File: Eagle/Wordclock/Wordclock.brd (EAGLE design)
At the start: 130 x 130 mm, 266 parts, among them IC1 MEGA8-P, Q3 SUP75N06-08

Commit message: layout der leds
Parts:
- added PAD3, PAD4: (no value), wirepad:2,54/1,1
- R1, R2: device rcl:M0805 -> rcl:R1206
- moved Q2 39.5 mm to (-2.74, 69.5), turned to 90 degrees
- moved SV1 34.0 mm to (7.23, 109.6), turned to 90 degrees
- moved R_LED4 20.4 mm to (33.0, 123.9)
- moved R1 18.6 mm to (50.3, 122.0)
- moved R2 17.8 mm to (43.0, 121.5), turned to 0 degrees
- moved Q1 11.6 mm to (52.3, 116.6)
- moved S+1 8.66 mm to (40.5, 120.2), turned to 0 degrees
- turned IC1 to 90 degrees
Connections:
- net GND: now also PAD4.1
- net VDD: now also PAD3.1
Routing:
- net SCL: track 0.00 -> 39.6 mm
- net SDA: track 0.00 -> 38.0 mm
- net SCHALTER1: track 38.5 -> 2.70 mm
- net +5V: track 244.0 -> 278.0 mm
- net GND: track 1683.2 -> 1654.1 mm
- net N$117: track 0.00 -> 21.7 mm
- net LEDMIN1: track 118.1 -> 136.0 mm
- net N$127: track 109.7 -> 124.8 mm
- net MATRIXIN: track 0.00 -> 14.3 mm
- net INTA: track 0.00 -> 13.6 mm
- net LEDALARM: track 46.6 -> 39.7 mm
- net LEDMIN4: track 0.00 -> 5.52 mm
- net N$20: track 11.0 -> 5.65 mm
- net INTB: track 0.00 -> 2.75 mm
- net N$21: track 16.4 -> 14.6 mm

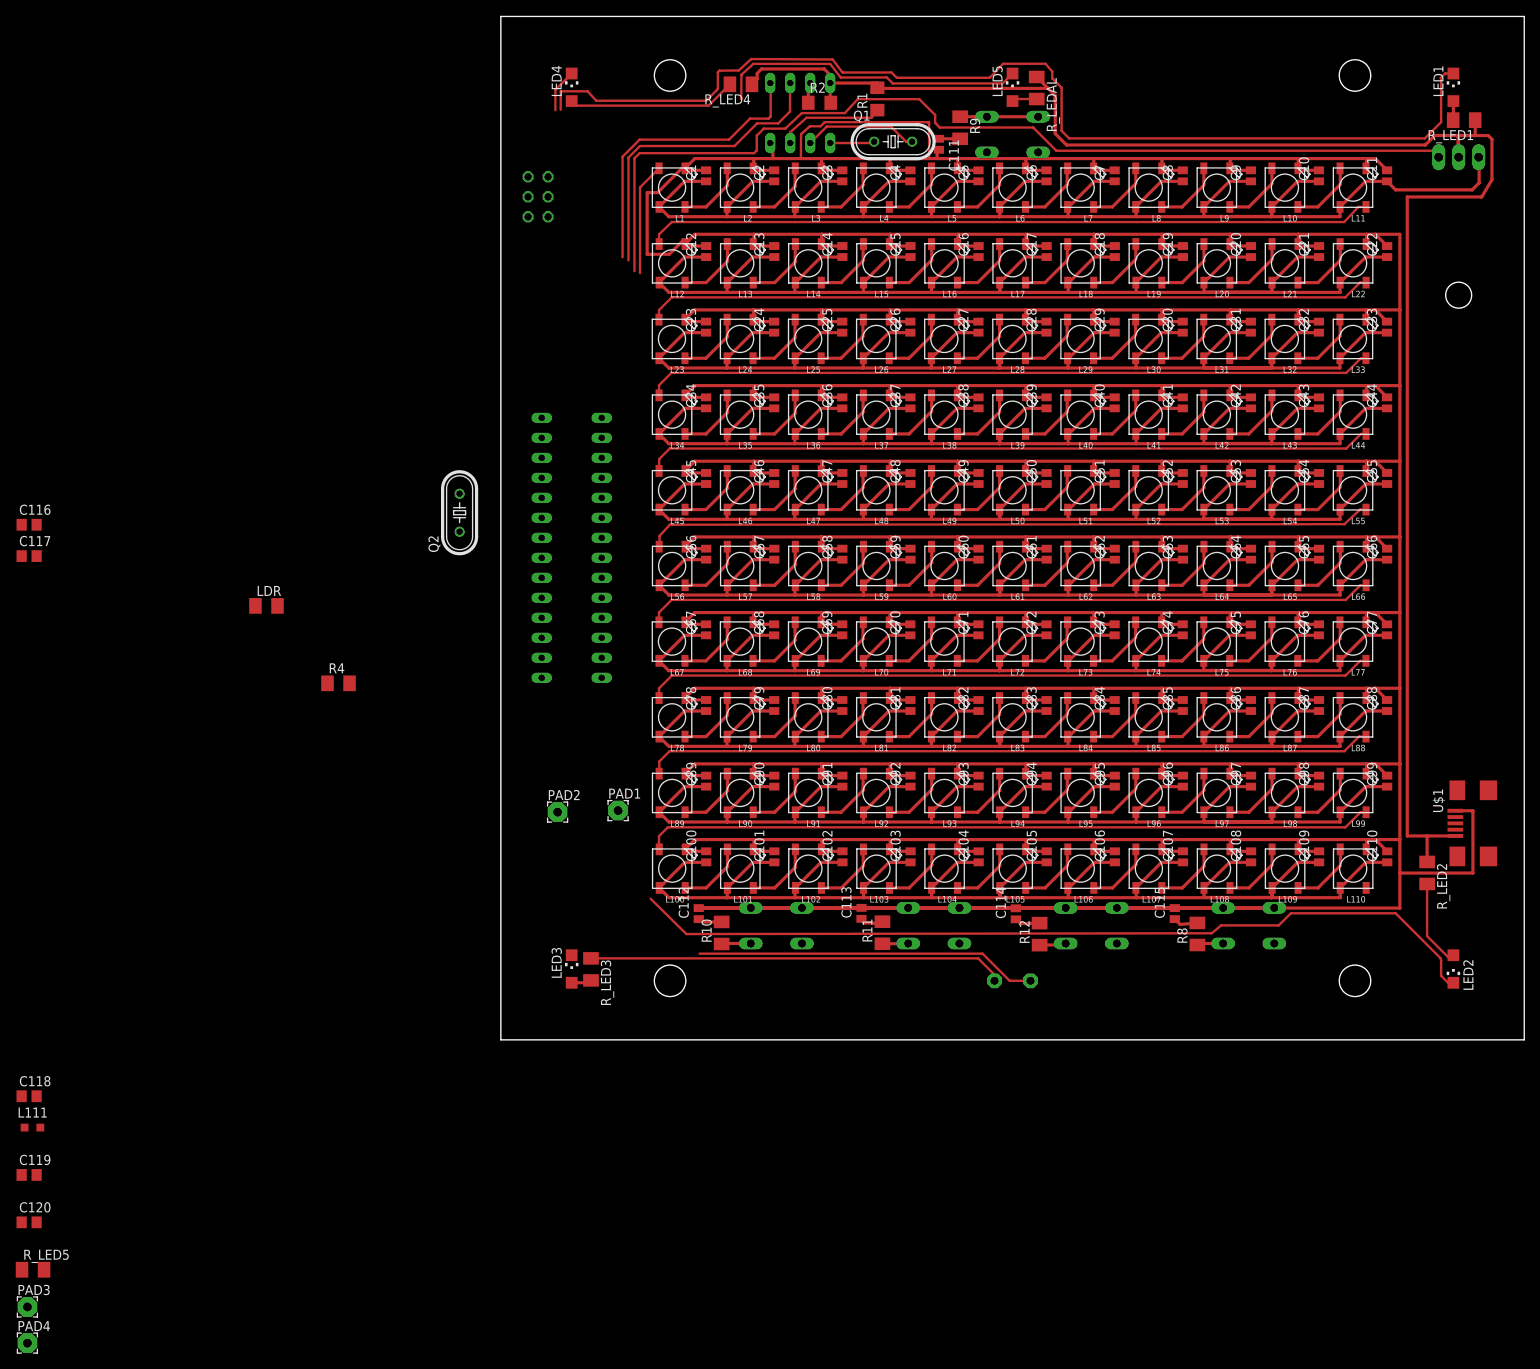
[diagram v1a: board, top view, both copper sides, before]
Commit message: Eagle untere hälfte der Platine und LED Layout fertig
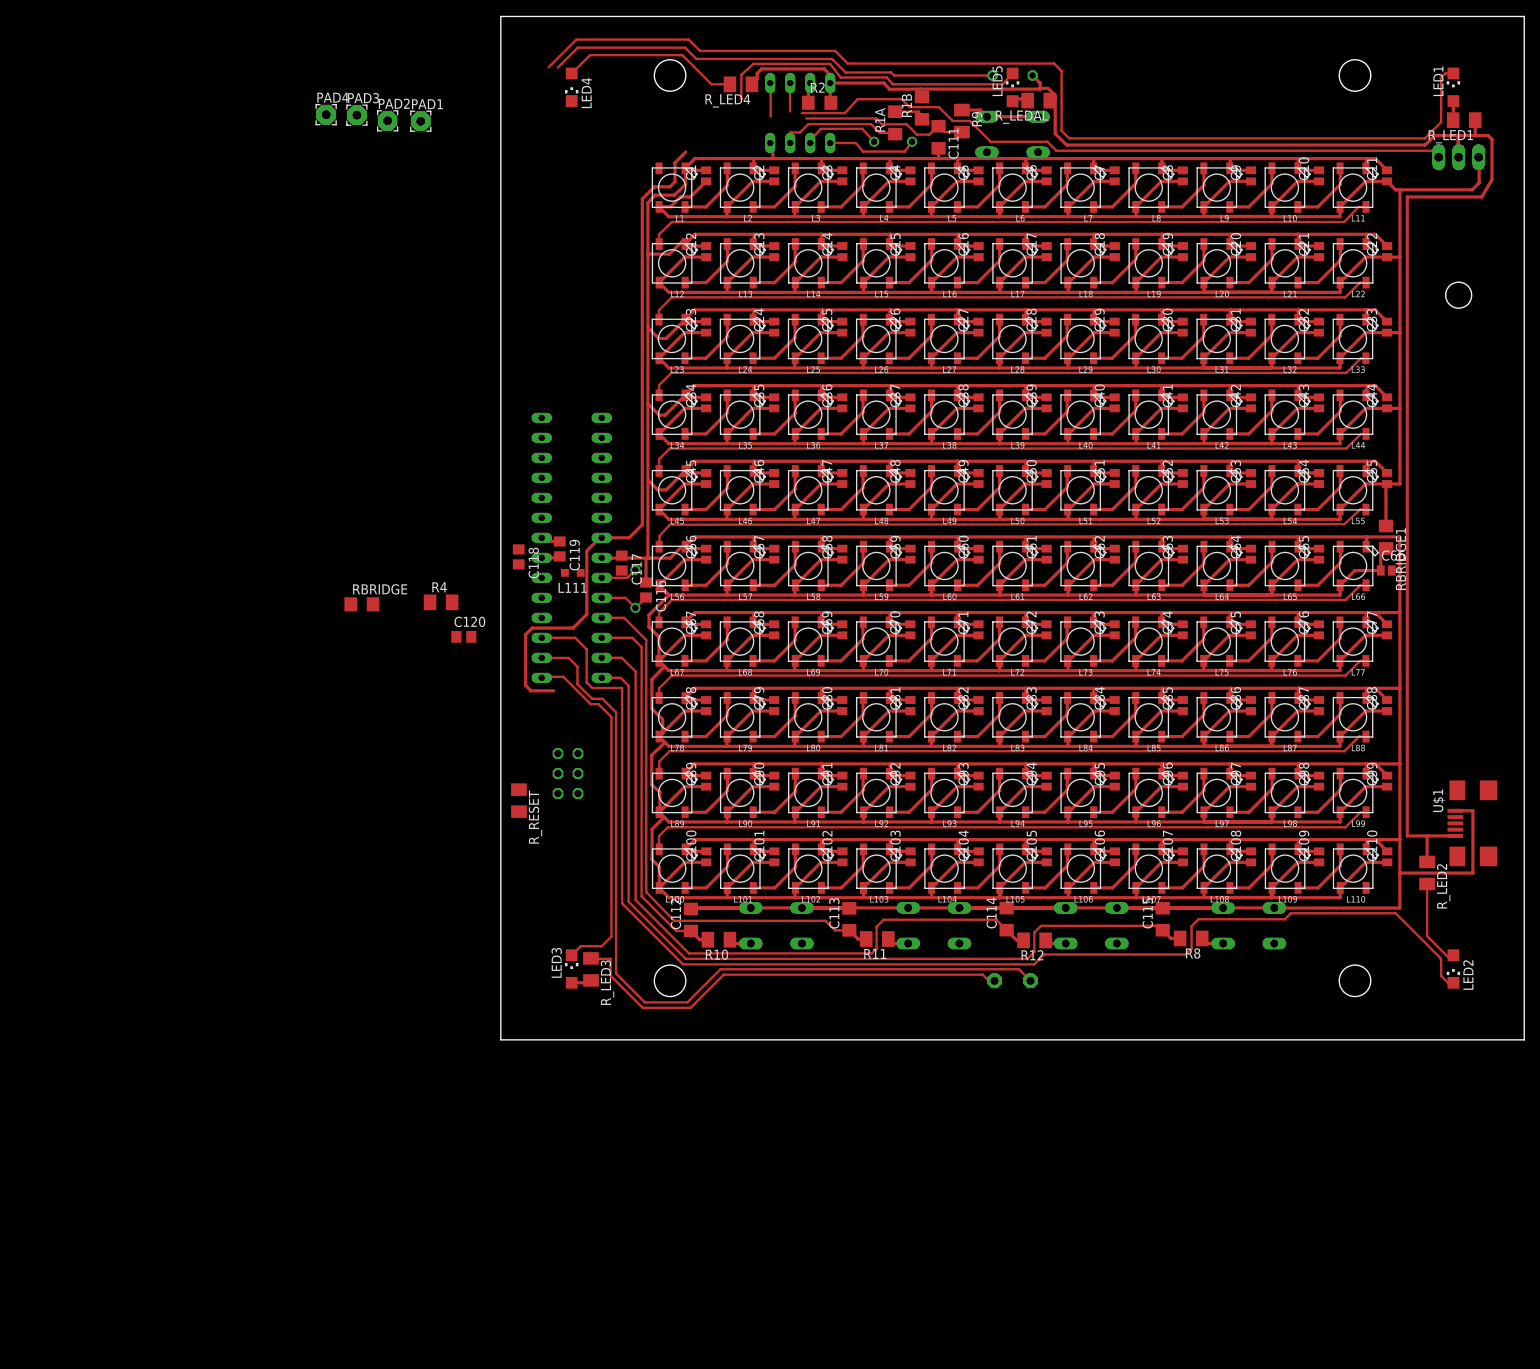
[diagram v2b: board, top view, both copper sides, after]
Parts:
- removed R1: (no value), rcl:R1206
- removed R_LED5: (no value), rcl:M1206
- added R1A, R1B, RBRIDGE, RBRIDGE1: (no value), rcl:R1206
- added R_RESET: (no value), rcl:M1206
- C111, C112, C113, C114, C115: device rcl:C1310 -> rcl:C1206
- LDR: device rcl:M1206 -> rcl:0204/5
- moved PAD4 160.6 mm to (-19.7, 120.0)
- moved PAD3 157.1 mm to (-15.8, 120.0)
- moved LDR 116.3 mm to (67.5, 125.0), flipped to the bottom, turned to 180 degrees
- moved C119 104.2 mm to (9.98, 64.9), turned to 270 degrees
- moved L111 98.4 mm to (11.6, 61.8), turned to 180 degrees
- moved C120 92.6 mm to (-2.20, 53.7)
- moved C118 92.5 mm to (4.77, 63.9), turned to 270 degrees
- moved PAD1 91.1 mm to (-7.67, 119.2)
- moved PAD2 90.4 mm to (-11.9, 119.2)
- moved C116 78.8 mm to (20.9, 59.6), turned to 270 degrees
- moved C117 75.3 mm to (17.9, 63.1), turned to 270 degrees
- moved SV1 73.4 mm to (11.0, 36.3)
- moved Q2 24.3 mm to (19.6, 59.8), flipped to the bottom, turned to 270 degrees
- moved R4 16.6 mm to (-5.09, 58.1)
- moved C66 2.08 mm to (115.0, 62.1), turned to 0 degrees
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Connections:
- net LDR renamed PHOTO
- net N$127 renamed MOSFET
- removed net N$112: IC1.2, SP1.-
- new net BUZZER: IC1.16, SP1.-
- new net N$124: R1A.2, R1B.1
- net +5V: now also PAD3.1, R1B.2, R_RESET.2; no longer R1.2, R_LED5.2
- net GND: now also RBRIDGE.1, RBRIDGE.2
- net INTA: now also R1A.1; no longer R1.1
- net LEDMIN1: now also IC1.18, SV1.1; no longer IC1.16
- net LEDMIN3: now also IC1.15; no longer IC1.18, SV1.1
- net NC1: now also IC1.2, PAD2.1; no longer IC1.14, PAD1.1
- net NC2: now also IC1.6, PAD1.1; no longer IC1.15, PAD2.1
- net RESET: now also R_RESET.1; no longer R_LED5.1
- net SCHALTER2: now also IC1.12; no longer IC1.6
- net SCHALTER4: now also IC1.13; no longer IC1.12
- net SCHALTER5: now also IC1.14; no longer IC1.13
- net VDD: now also RBRIDGE1.1, RBRIDGE1.2; no longer PAD3.1
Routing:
- net SCHALTER5: track 3.16 -> 108.2 mm
- net BUZZER: track 0.00 -> 103.3 mm
- net +5V: track 278.0 -> 370.2 mm
- net VDD: track 1929.7 -> 2020.3 mm
- net SCHALTER4: track 3.22 -> 90.6 mm
- net SCHALTER3: track 3.08 -> 69.3 mm
- net PHOTO: track 0.00 -> 57.7 mm
- net LEDMIN2: track 109.7 -> 160.8 mm
- net LEDMIN3: track 0.00 -> 44.9 mm
- net SCHALTER2: track 3.02 -> 47.9 mm
- net N$112: track 43.5 -> 0.00 mm
- net MOSFET: track 124.8 -> 85.2 mm
- net SCL: track 39.6 -> 3.62 mm
- net GND: track 1654.1 -> 1620.1 mm
- net SDA: track 38.0 -> 4.29 mm
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
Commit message: Layout fertig
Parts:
- removed R1A, R1B: (no value), rcl:R1206
- added BRIDGE_RESET: (no value), rcl:M1206
- added R1, R6, R7, RBRIDGE2, RBRIDGE3, RBRIDGE4, RBRIDGE5, R_MOSFET: (no value), rcl:R1206
- C118: device rcl:C0805 -> rcl:C1206
- moved R4 94.9 mm to (60.7, 126.5), turned to 270 degrees
- moved R_RESET 75.7 mm to (16.2, 107.8), turned to 180 degrees
- moved PAD4 41.1 mm to (15.0, 98.0)
- moved PAD3 39.7 mm to (15.0, 95.0)
- moved PAD1 35.4 mm to (15.0, 92.0)
- moved PAD2 32.5 mm to (15.0, 101.0)
- moved RBRIDGE 28.9 mm to (12.8, 65.3), turned to 270 degrees
- moved C120 25.3 mm to (20.0, 65.9), turned to 90 degrees
- moved C118 7.04 mm to (11.5, 61.8), turned to 180 degrees
- moved L111 4.78 mm to (12.0, 57.1), turned to 90 degrees
- moved R_LED4 1.43 mm to (33.1, 125.3)
- moved SV1 0.82 mm to (11.5, 37.0), turned to 180 degrees
- moved R10 0.69 mm to (30.2, 15.9)
- moved C119 0.12 mm to (10.0, 65.0)
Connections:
- removed net MOSFET: IC1.24, Q3.1
- new net INTB_UNBRIDGED: R2.1, RBRIDGE3.2, S+1.7
- new net MOSFET_A: IC1.24, R_MOSFET.1
- new net MOSFET_B: Q3.1, R_MOSFET.2
- new net N$112: R6.2, S+1.6
- new net N$125: BRIDGE_RESET.1, IC1.1, R_RESET.1
- new net N$127: RBRIDGE2.1, SV1.4
- new net N$128: RBRIDGE4.1, SV1.3
- new net N$129: RBRIDGE5.1, SV1.5
- net +5V: now also R1.2; no longer R1B.2
- net INTA: now also IC1.5, R1.1; no longer IC1.4, R1A.1
- net INTB: now also IC1.4, RBRIDGE3.1; no longer IC1.5, R2.1, S+1.7
- net LEDALARM: now also IC1.26; no longer IC1.23
- net LEDMIN2: now also RBRIDGE2.2; no longer SV1.4
- net LEDMIN4: now also RBRIDGE4.2; no longer SV1.3
- net MATRIXIN: now also IC1.2; no longer IC1.25
- net N$124: now also R7.2, S+1.5; no longer R1A.2, R1B.1
- net NC1: now also IC1.23; no longer IC1.2
- net PHOTO: now also IC1.25; no longer IC1.26
- net RESET: now also BRIDGE_RESET.2, RBRIDGE5.2; no longer IC1.1, R_RESET.1, SV1.5
- net SCL: now also R6.1; no longer S+1.6
- net SDA: now also R7.1; no longer S+1.5
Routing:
- net GND: track 1620.1 -> 2032.3 mm
- net LEDMIN1: track 132.8 -> 247.4 mm
- net MOSFET_B: track 0.00 -> 113.9 mm
- net LEDMIN4: track 0.00 -> 90.7 mm
- net +5V: track 370.2 -> 459.1 mm
- net MOSFET: track 85.2 -> 0.00 mm
- net LEDMIN2: track 160.8 -> 240.9 mm
- net LEDALARM: track 39.9 -> 118.0 mm
- net RESET: track 0.00 -> 74.6 mm
- net SCHALTER1: track 21.4 -> 88.7 mm
- net PHOTO: track 57.7 -> 124.6 mm
- net MOSFET_A: track 0.00 -> 61.5 mm
- net INTA: track 15.7 -> 68.6 mm
- net SDA: track 4.29 -> 55.3 mm
- net INTB: track 2.75 -> 52.1 mm
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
